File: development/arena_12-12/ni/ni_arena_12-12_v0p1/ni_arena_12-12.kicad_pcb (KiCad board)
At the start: 4 copper layers, 228.6 x 228.6 mm, 54 parts, among them J1 Barrel_Jack, J2 NI_TE_68pos, P1 CONN15, P10 CONN15, P11 CONN15, P12 CONN15, P2 CONN15, P3 CONN15, P4 CONN15, P5 CONN15, P6 CONN15, P7 CONN15, P8 CONN15, P9 CONN15, Q2 MOSFET_NCHAN, SW1 SW_SPDT, U1 TXB0108PW, U2 TXB0108PW, U3 TXB0108PW, U4 TXB0108PW, U5 TXB0108PW, U6 AP2112K-3.3

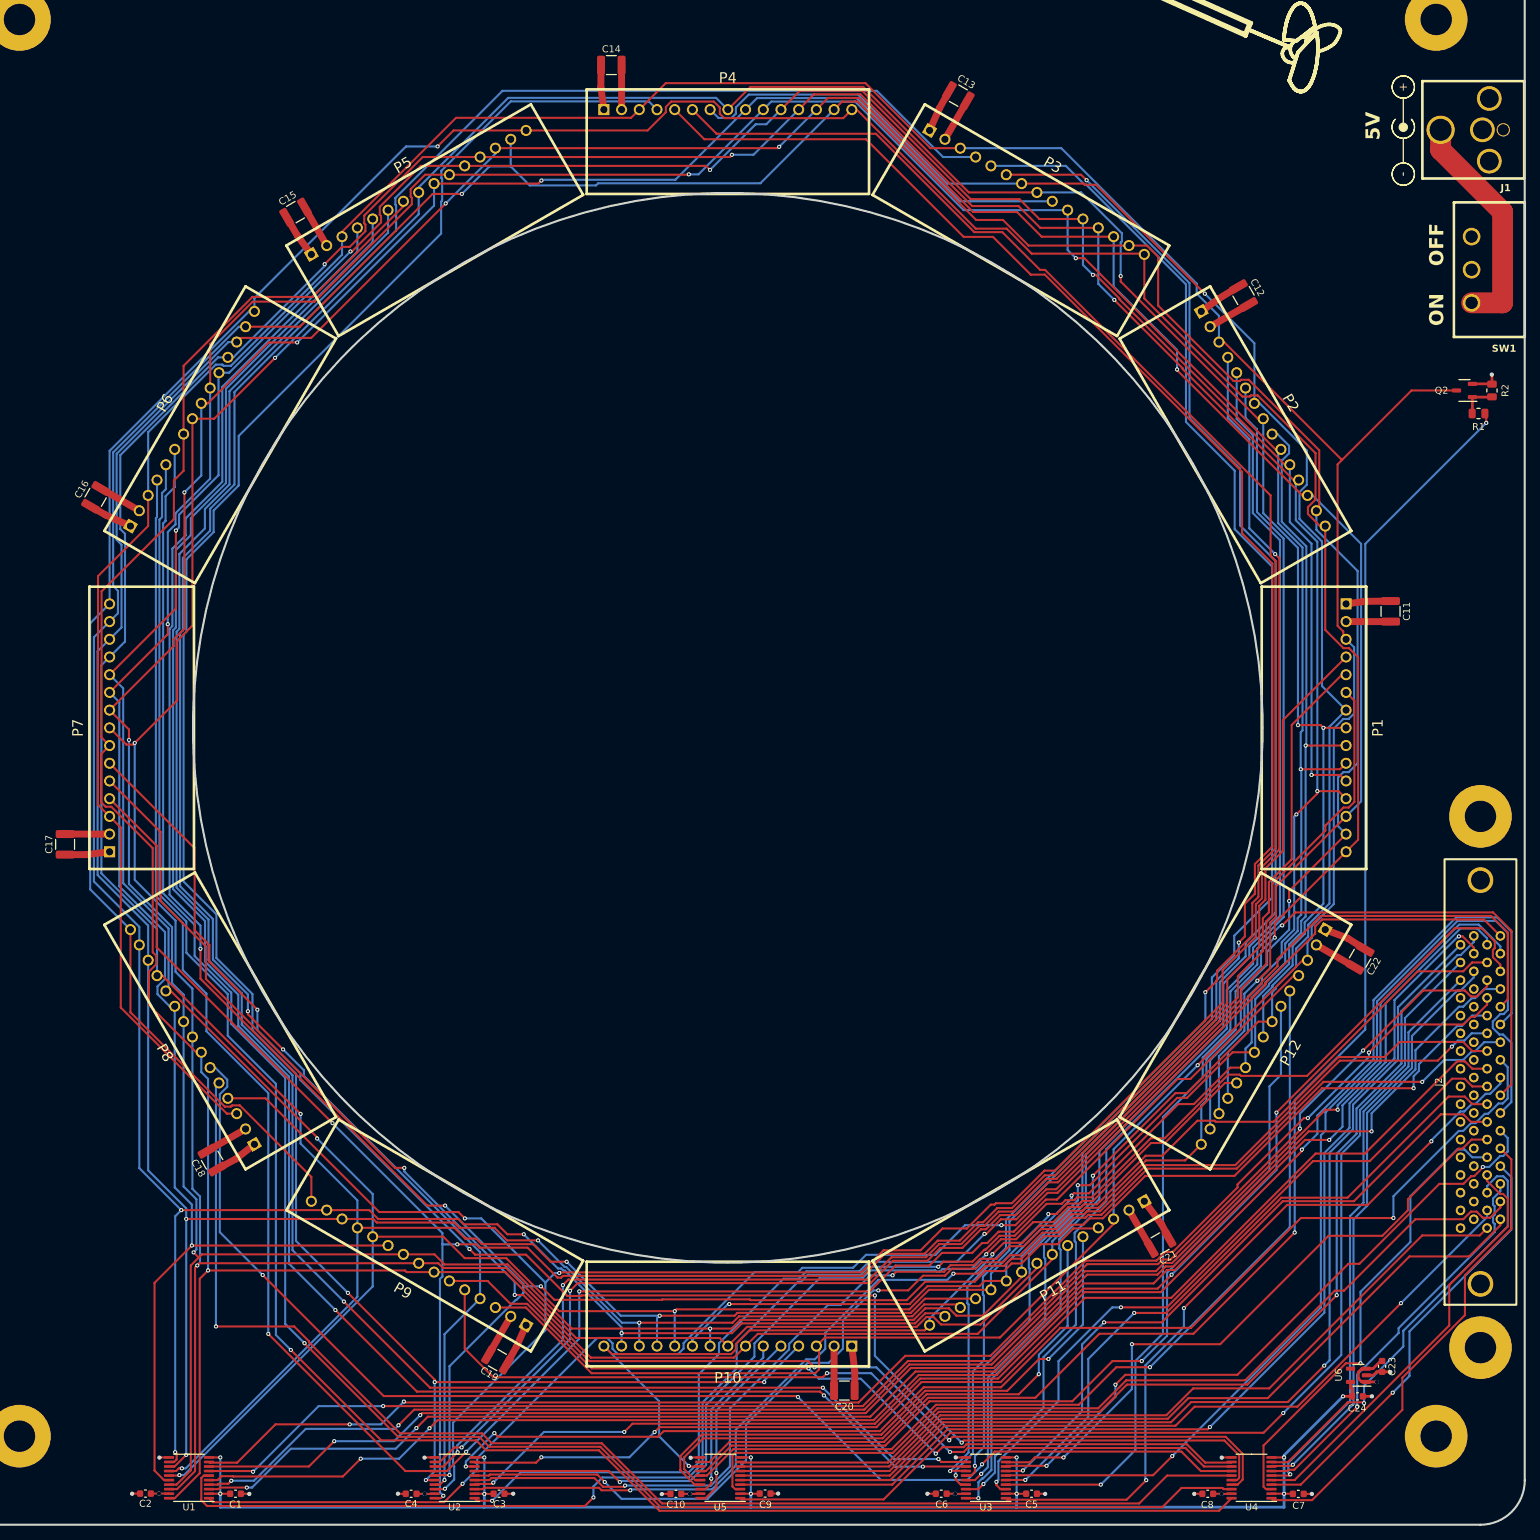
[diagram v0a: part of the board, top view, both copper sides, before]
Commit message: Worked on schematic adding series termination resistors and buffers.
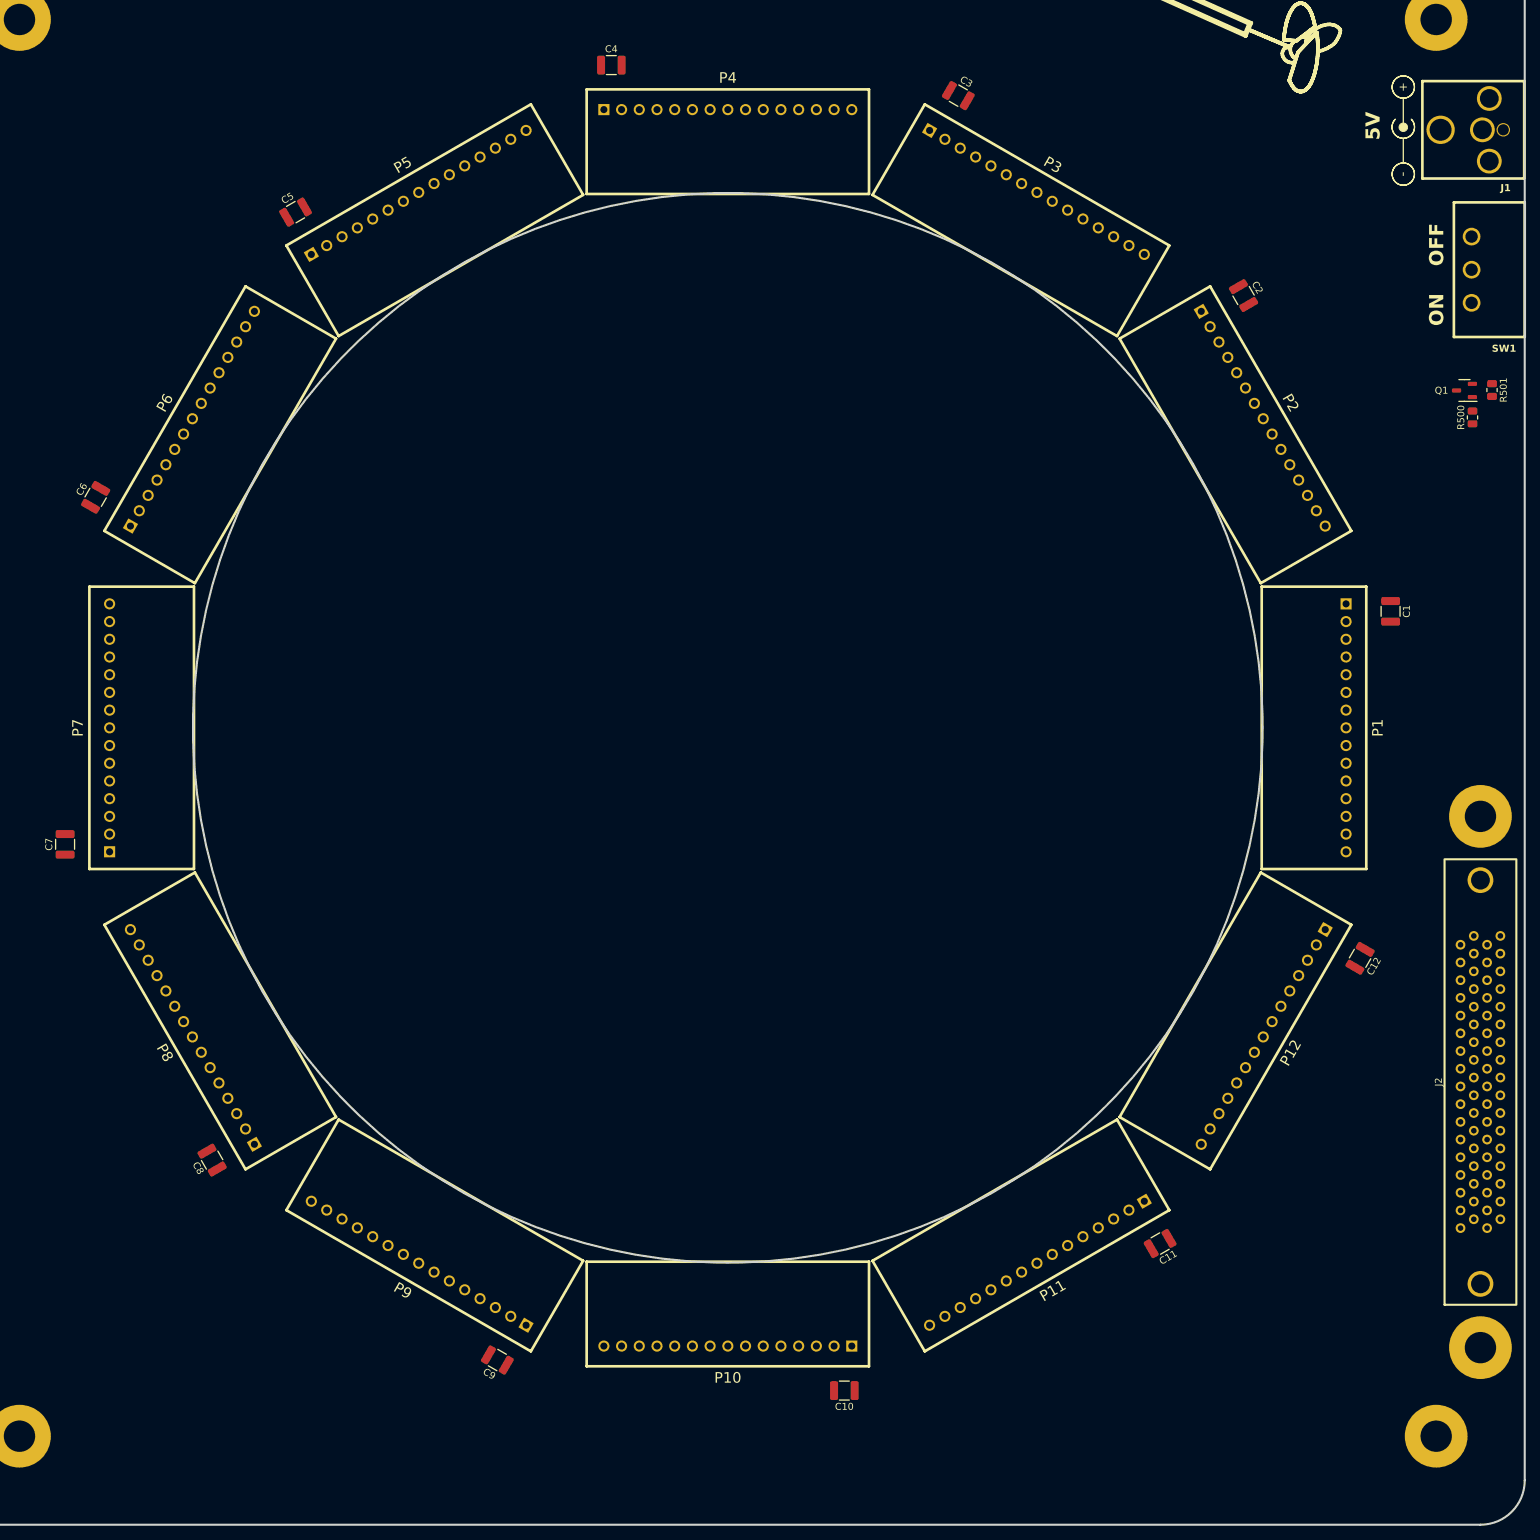
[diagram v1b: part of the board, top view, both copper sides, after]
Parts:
- removed the C1 at (107.2, 287.7)
- removed the C10 at (170.3, 287.7)
- removed the C2 at (94.3, 287.6)
- removed C23, C24: 10uF, Capacitor_SMD:C_0603_1608Metric
- removed the C3 at (145.0, 287.7)
- removed the C4 at (132.4, 287.7)
- removed the C5 at (221.4, 287.7)
- removed the C6 at (208.4, 287.7)
- removed the C7 at (259.6, 287.7)
- removed the C8 at (246.6, 287.7)
- removed the C9 at (183.1, 287.6)
- removed R1: 200, Resistor_SMD:R_0805_2012Metric
- removed R2: 20k, Resistor_SMD:R_0805_2012Metric
- removed U1, U2, U3, U4, U5: TXB0108PW, Package_SO:TSSOP-20_4.4x6.5mm_P0.65mm
- removed U6: AP2112K-3.3, Package_TO_SOT_SMD:SOT-23-5
- added R500: 200, Resistor_SMD:R_0805_2012Metric, F.Cu at (284.6, 133.3)
- added R501: 20k, Resistor_SMD:R_0805_2012Metric, F.Cu at (287.4, 129.3)
- renumbered C11 to C1, C20 to C10, C21 to C11, C22 to C12, C12 to C2, C13 to C3, C14 to C4, C15 to C5, C16 to C6, C17 to C7, C18 to C8, C19 to C9, Q2 to Q1
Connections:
- net Net-(SW1-A) renamed /Power & Voltage Regulators/SW_5V
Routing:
- net /Level Shifters/PAN5V.CS_07: track 608.7 -> 0.00 mm, vias 6 -> 0
- net /Level Shifters/PAN5V.CS_00: track 605.9 -> 0.00 mm, vias 3 -> 0
- net /Level Shifters/PAN5V.CS_01: track 601.7 -> 0.00 mm, vias 6 -> 0
- net /Level Shifters/PAN5V.CS_03: track 599.0 -> 0.00 mm, vias 7 -> 0
- net /Level Shifters/PAN5V.CS_06: track 598.2 -> 0.00 mm, vias 8 -> 0
- net /Level Shifters/PAN5V.CS_02: track 596.4 -> 0.00 mm, vias 8 -> 0
- net /Level Shifters/PAN5V.CS_05: track 594.7 -> 0.00 mm, vias 9 -> 0
- net /Level Shifters/PAN5V.CS_04: track 592.5 -> 0.00 mm, vias 9 -> 0
- net /Level Shifters/PAN5V.EXT_INT: track 581.4 -> 0.00 mm, vias 4 -> 0
- net /Panel Headers/RESET: track 579.7 -> 0.00 mm, vias 1 -> 0
- net /Level Shifters/PAN5V.SCK_05: track 318.6 -> 0.00 mm, vias 3 -> 0
- net /Level Shifters/PAN5V.SCK_02: track 311.9 -> 0.00 mm, vias 3 -> 0
- net /Level Shifters/PAN5V.SCK_03: track 309.9 -> 0.00 mm, vias 4 -> 0
- net /Level Shifters/PAN5V.SCK_00: track 309.1 -> 0.00 mm, vias 3 -> 0
- net /Level Shifters/PAN5V.SCK_04: track 306.8 -> 0.00 mm, vias 4 -> 0
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
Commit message: Wored on layout for 12-12 NI arena with schmitt buffers.
Worked on layout for schmitt buffers and series term. resitors around
at the base of a panel column.
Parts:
- removed R500: 200, Resistor_SMD:R_0805_2012Metric
- removed R501: 20k, Resistor_SMD:R_0805_2012Metric
- added C100: 0.1uF, Capacitor_SMD:C_0402_1005Metric, F.Cu at (422.1, 25.1)
- added C101: 0.1uF, Capacitor_SMD:C_0402_1005Metric, F.Cu at (422.1, 27.1)
- added C102: 0.1uF, Capacitor_SMD:C_0402_1005Metric, F.Cu at (422.1, 29.0)
- added C103: 0.1uF, Capacitor_SMD:C_0402_1005Metric, F.Cu at (422.1, 31.0)
- added C104: 0.1uF, Capacitor_SMD:C_0402_1005Metric, F.Cu at (422.1, 33.0)
- added C105: 0.1uF, Capacitor_SMD:C_0402_1005Metric, F.Cu at (422.1, 34.9)
- added C106: 0.1uF, Capacitor_SMD:C_0402_1005Metric, F.Cu at (422.1, 36.9)
- added C107: 0.1uF, Capacitor_SMD:C_0402_1005Metric, F.Cu at (458.9, 5.04)
- added C108: 0.1uF, Capacitor_SMD:C_0402_1005Metric, F.Cu at (458.9, 7.01)
- added C109: 0.1uF, Capacitor_SMD:C_0402_1005Metric, F.Cu at (458.9, 8.98)
- added C110: 0.1uF, Capacitor_SMD:C_0402_1005Metric, F.Cu at (458.9, 10.9)
- added C111: 0.1uF, Capacitor_SMD:C_0402_1005Metric, F.Cu at (458.9, 12.9)
- added C112: 0.1uF, Capacitor_SMD:C_0402_1005Metric, F.Cu at (458.9, 14.9)
- added C113: 0.1uF, Capacitor_SMD:C_0402_1005Metric, F.Cu at (458.9, 16.9)
- added C114: 0.1uF, Capacitor_SMD:C_0402_1005Metric, F.Cu at (458.9, 18.8)
- added C115: 0.1uF, Capacitor_SMD:C_0402_1005Metric, F.Cu at (458.9, 20.8)
- added C116: 0.1uF, Capacitor_SMD:C_0402_1005Metric, F.Cu at (458.9, 22.8)
- added C117: 0.1uF, Capacitor_SMD:C_0402_1005Metric, F.Cu at (461.8, 5.04)
- added C118: 0.1uF, Capacitor_SMD:C_0402_1005Metric, F.Cu at (461.8, 7.01)
- added C119: 0.1uF, Capacitor_SMD:C_0402_1005Metric, F.Cu at (461.8, 8.98)
- added C120: 0.1uF, Capacitor_SMD:C_0402_1005Metric, F.Cu at (461.8, 10.9)
- added C121: 0.1uF, Capacitor_SMD:C_0402_1005Metric, F.Cu at (461.8, 12.9)
- added C122: 0.1uF, Capacitor_SMD:C_0402_1005Metric, F.Cu at (461.8, 14.9)
- added C123: 0.1uF, Capacitor_SMD:C_0402_1005Metric, F.Cu at (461.8, 16.9)
- added C124: 0.1uF, Capacitor_SMD:C_0402_1005Metric, F.Cu at (461.8, 18.8)
- added C125: 0.1uF, Capacitor_SMD:C_0402_1005Metric, F.Cu at (461.8, 20.8)
- added C126: 0.1uF, Capacitor_SMD:C_0402_1005Metric, F.Cu at (461.8, 22.8)
- added C127: 0.1uF, Capacitor_SMD:C_0402_1005Metric, F.Cu at (464.7, 5.04)
- added C128: 0.1uF, Capacitor_SMD:C_0402_1005Metric, F.Cu at (464.7, 7.01)
- added C129: 0.1uF, Capacitor_SMD:C_0402_1005Metric, F.Cu at (464.7, 8.98)
- added C13: 10uF, Capacitor_SMD:C_1206_3216Metric, F.Cu at (443.7, 44.0)
- added C130: 0.1uF, Capacitor_SMD:C_0402_1005Metric, F.Cu at (464.7, 10.9)
- added C131: 0.1uF, Capacitor_SMD:C_0402_1005Metric, F.Cu at (464.7, 12.9)
- added C132: 0.1uF, Capacitor_SMD:C_0402_1005Metric, F.Cu at (464.7, 14.9)
- added C133: 0.1uF, Capacitor_SMD:C_0402_1005Metric, F.Cu at (464.7, 16.9)
- added C134: 0.1uF, Capacitor_SMD:C_0402_1005Metric, F.Cu at (464.7, 18.8)
- added C135: 0.1uF, Capacitor_SMD:C_0402_1005Metric, F.Cu at (464.7, 20.8)
- added C136: 0.1uF, Capacitor_SMD:C_0402_1005Metric, F.Cu at (464.7, 22.8)
- added C137: 0.1uF, Capacitor_SMD:C_0402_1005Metric, F.Cu at (467.6, 5.04)
- added C138: 0.1uF, Capacitor_SMD:C_0402_1005Metric, F.Cu at (467.6, 7.01)
- added C139: 0.1uF, Capacitor_SMD:C_0402_1005Metric, F.Cu at (467.6, 8.98)
- added C14: 10uF, Capacitor_SMD:C_1206_3216Metric, F.Cu at (443.7, 47.3)
- added C140: 0.1uF, Capacitor_SMD:C_0402_1005Metric, F.Cu at (467.6, 10.9)
- added C15: 0.1uF, Capacitor_SMD:C_0402_1005Metric, F.Cu at (453.2, 5.04)
- added C16: 0.1uF, Capacitor_SMD:C_0402_1005Metric, F.Cu at (453.2, 7.01)
- added C17: 0.1uF, Capacitor_SMD:C_0402_1005Metric, F.Cu at (453.2, 8.98)
- added C18: 0.1uF, Capacitor_SMD:C_0402_1005Metric, F.Cu at (453.2, 10.9)
- added C19: 0.1uF, Capacitor_SMD:C_0402_1005Metric, F.Cu at (453.2, 12.9)
- added C20: 0.1uF, Capacitor_SMD:C_0402_1005Metric, F.Cu at (453.2, 14.9)
- added C21: 0.1uF, Capacitor_SMD:C_0402_1005Metric, F.Cu at (453.2, 16.9)
- added C22: 0.1uF, Capacitor_SMD:C_0402_1005Metric, F.Cu at (453.2, 18.8)
- added C23: 0.1uF, Capacitor_SMD:C_0402_1005Metric, F.Cu at (453.2, 20.8)
- added C24: 0.1uF, Capacitor_SMD:C_0402_1005Metric, F.Cu at (453.2, 22.8)
- added C25: 0.1uF, Capacitor_SMD:C_0402_1005Metric, F.Cu at (456.1, 5.04)
- added C26: 0.1uF, Capacitor_SMD:C_0402_1005Metric, F.Cu at (456.1, 7.01)
- added C27: 0.1uF, Capacitor_SMD:C_0402_1005Metric, F.Cu at (456.1, 8.98)
- added C28: 0.1uF, Capacitor_SMD:C_0402_1005Metric, F.Cu at (456.1, 10.9)
- added C29: 0.1uF, Capacitor_SMD:C_0402_1005Metric, F.Cu at (456.1, 12.9)
- added C30: 0.1uF, Capacitor_SMD:C_0402_1005Metric, F.Cu at (456.1, 14.9)
- added C31: 0.1uF, Capacitor_SMD:C_0402_1005Metric, F.Cu at (456.1, 16.9)
- added C32: 0.1uF, Capacitor_SMD:C_0402_1005Metric, F.Cu at (456.1, 18.8)
- added C33: 0.1uF, Capacitor_SMD:C_0402_1005Metric, F.Cu at (456.1, 20.8)
- added C34: 0.1uF, Capacitor_SMD:C_0402_1005Metric, F.Cu at (456.1, 22.8)
- added C35: 0.1uF, Capacitor_SMD:C_0402_1005Metric, F.Cu at (271.1, 168.9)
- added C36: 0.1uF, Capacitor_SMD:C_0402_1005Metric, F.Cu at (271.1, 176.6)
- added C37: 0.1uF, Capacitor_SMD:C_0402_1005Metric, F.Cu at (271.1, 181.7)
- added C38: 0.1uF, Capacitor_SMD:C_0402_1005Metric, F.Cu at (271.1, 186.7)
- added C39: 0.1uF, Capacitor_SMD:C_0402_1005Metric, F.Cu at (271.0, 191.8)
- added C40: 0.1uF, Capacitor_SMD:C_0402_1005Metric, F.Cu at (271.0, 197.3)
- added C41: 0.1uF, Capacitor_SMD:C_0402_1005Metric, F.Cu at (407.7, 27.1)
- added C42: 0.1uF, Capacitor_SMD:C_0402_1005Metric, F.Cu at (407.7, 29.0)
- added C43: 0.1uF, Capacitor_SMD:C_0402_1005Metric, F.Cu at (407.7, 31.0)
- added C44: 0.1uF, Capacitor_SMD:C_0402_1005Metric, F.Cu at (407.7, 33.0)
- added C45: 0.1uF, Capacitor_SMD:C_0402_1005Metric, F.Cu at (407.7, 34.9)
- added C46: 0.1uF, Capacitor_SMD:C_0402_1005Metric, F.Cu at (407.7, 36.9)
- added C47: 0.1uF, Capacitor_SMD:C_0402_1005Metric, F.Cu at (410.6, 15.2)
- added C48: 0.1uF, Capacitor_SMD:C_0402_1005Metric, F.Cu at (410.6, 17.2)
- added C49: 0.1uF, Capacitor_SMD:C_0402_1005Metric, F.Cu at (410.6, 19.2)
- added C50: 0.1uF, Capacitor_SMD:C_0402_1005Metric, F.Cu at (410.6, 21.1)
- added C51: 0.1uF, Capacitor_SMD:C_0402_1005Metric, F.Cu at (410.6, 23.1)
- added C52: 0.1uF, Capacitor_SMD:C_0402_1005Metric, F.Cu at (410.6, 25.1)
- added C53: 0.1uF, Capacitor_SMD:C_0402_1005Metric, F.Cu at (410.6, 27.1)
- added C54: 0.1uF, Capacitor_SMD:C_0402_1005Metric, F.Cu at (410.6, 29.0)
- added C55: 0.1uF, Capacitor_SMD:C_0402_1005Metric, F.Cu at (410.6, 31.0)
- added C56: 0.1uF, Capacitor_SMD:C_0402_1005Metric, F.Cu at (410.6, 33.0)
- added C57: 0.1uF, Capacitor_SMD:C_0402_1005Metric, F.Cu at (410.6, 34.9)
- added C58: 0.1uF, Capacitor_SMD:C_0402_1005Metric, F.Cu at (410.6, 36.9)
- added C59: 0.1uF, Capacitor_SMD:C_0402_1005Metric, F.Cu at (413.5, 15.2)
- added C60: 0.1uF, Capacitor_SMD:C_0402_1005Metric, F.Cu at (413.5, 17.2)
- added C61: 0.1uF, Capacitor_SMD:C_0402_1005Metric, F.Cu at (413.5, 19.2)
- added C62: 0.1uF, Capacitor_SMD:C_0402_1005Metric, F.Cu at (413.5, 21.1)
- added C63: 0.1uF, Capacitor_SMD:C_0402_1005Metric, F.Cu at (413.5, 23.1)
- added C64: 0.1uF, Capacitor_SMD:C_0402_1005Metric, F.Cu at (413.5, 25.1)
- added C65: 0.1uF, Capacitor_SMD:C_0402_1005Metric, F.Cu at (413.5, 27.1)
- added C66: 0.1uF, Capacitor_SMD:C_0402_1005Metric, F.Cu at (413.5, 29.0)
- added C67: 0.1uF, Capacitor_SMD:C_0402_1005Metric, F.Cu at (413.5, 31.0)
- added C68: 0.1uF, Capacitor_SMD:C_0402_1005Metric, F.Cu at (413.5, 33.0)
- added C69: 0.1uF, Capacitor_SMD:C_0402_1005Metric, F.Cu at (413.5, 34.9)
- added C70: 0.1uF, Capacitor_SMD:C_0402_1005Metric, F.Cu at (413.5, 36.9)
- added C71: 0.1uF, Capacitor_SMD:C_0402_1005Metric, F.Cu at (416.4, 15.2)
- added C72: 0.1uF, Capacitor_SMD:C_0402_1005Metric, F.Cu at (416.4, 17.2)
- added C73: 0.1uF, Capacitor_SMD:C_0402_1005Metric, F.Cu at (416.4, 19.2)
- added C74: 0.1uF, Capacitor_SMD:C_0402_1005Metric, F.Cu at (416.4, 21.1)
- added C75: 0.1uF, Capacitor_SMD:C_0402_1005Metric, F.Cu at (416.4, 23.1)
- added C76: 0.1uF, Capacitor_SMD:C_0402_1005Metric, F.Cu at (416.4, 25.1)
- added C77: 0.1uF, Capacitor_SMD:C_0402_1005Metric, F.Cu at (416.4, 27.1)
- added C78: 0.1uF, Capacitor_SMD:C_0402_1005Metric, F.Cu at (416.4, 29.0)
- added C79: 0.1uF, Capacitor_SMD:C_0402_1005Metric, F.Cu at (416.4, 31.0)
- added C80: 0.1uF, Capacitor_SMD:C_0402_1005Metric, F.Cu at (416.4, 33.0)
- added C81: 0.1uF, Capacitor_SMD:C_0402_1005Metric, F.Cu at (416.4, 34.9)
- added C82: 0.1uF, Capacitor_SMD:C_0402_1005Metric, F.Cu at (416.4, 36.9)
- added C83: 0.1uF, Capacitor_SMD:C_0402_1005Metric, F.Cu at (419.2, 15.2)
- added C84: 0.1uF, Capacitor_SMD:C_0402_1005Metric, F.Cu at (419.2, 17.2)
- added C85: 0.1uF, Capacitor_SMD:C_0402_1005Metric, F.Cu at (419.2, 19.2)
- added C86: 0.1uF, Capacitor_SMD:C_0402_1005Metric, F.Cu at (419.2, 21.1)
- added C87: 0.1uF, Capacitor_SMD:C_0402_1005Metric, F.Cu at (419.2, 23.1)
- added C88: 0.1uF, Capacitor_SMD:C_0402_1005Metric, F.Cu at (419.2, 25.1)
- added C89: 0.1uF, Capacitor_SMD:C_0402_1005Metric, F.Cu at (419.2, 27.1)
- added C90: 0.1uF, Capacitor_SMD:C_0402_1005Metric, F.Cu at (419.2, 29.0)
- added C91: 0.1uF, Capacitor_SMD:C_0402_1005Metric, F.Cu at (419.2, 31.0)
- added C92: 0.1uF, Capacitor_SMD:C_0402_1005Metric, F.Cu at (419.2, 33.0)
- added C93: 0.1uF, Capacitor_SMD:C_0402_1005Metric, F.Cu at (419.2, 34.9)
- added C94: 0.1uF, Capacitor_SMD:C_0402_1005Metric, F.Cu at (419.2, 36.9)
- added C95: 0.1uF, Capacitor_SMD:C_0402_1005Metric, F.Cu at (422.1, 15.2)
- added C96: 0.1uF, Capacitor_SMD:C_0402_1005Metric, F.Cu at (422.1, 17.2)
- added C97: 0.1uF, Capacitor_SMD:C_0402_1005Metric, F.Cu at (422.1, 19.2)
- added C98: 0.1uF, Capacitor_SMD:C_0402_1005Metric, F.Cu at (422.1, 21.1)
- added C99: 0.1uF, Capacitor_SMD:C_0402_1005Metric, F.Cu at (422.1, 23.1)
- added J3: Barrel_Jack, arena_custom:DCJACK_2PIN_HIGHCURRENT, F.Cu at (95.0, 63.5)
- added R1: 33, Resistor_SMD:R_0402_1005Metric, F.Cu at (450.0, 43.3)
- added R10: 33, Resistor_SMD:R_0402_1005Metric, F.Cu at (452.9, 45.3)
- added R100: 33, Resistor_SMD:R_0402_1005Metric, F.Cu at (462.0, 3.06)
- added R101: 33, Resistor_SMD:R_0402_1005Metric, F.Cu at (464.9, -24.8)
- added R102: 33, Resistor_SMD:R_0402_1005Metric, F.Cu at (464.9, -22.8)
- added R103: 33, Resistor_SMD:R_0402_1005Metric, F.Cu at (464.9, -20.8)
- added R104: 33, Resistor_SMD:R_0402_1005Metric, F.Cu at (464.9, -18.8)
- added R105: 33, Resistor_SMD:R_0402_1005Metric, F.Cu at (464.9, -16.8)
- added R106: 33, Resistor_SMD:R_0402_1005Metric, F.Cu at (464.9, -14.8)
- added R107: 33, Resistor_SMD:R_0402_1005Metric, F.Cu at (464.9, -12.9)
- added R108: 33, Resistor_SMD:R_0402_1005Metric, F.Cu at (464.9, -10.9)
- added R109: 33, Resistor_SMD:R_0402_1005Metric, F.Cu at (464.9, -8.88)
- added R11: 33, Resistor_SMD:R_0402_1005Metric, F.Cu at (452.9, 47.3)
- added R110: 33, Resistor_SMD:R_0402_1005Metric, F.Cu at (464.9, -6.89)
- added R111: 33, Resistor_SMD:R_0402_1005Metric, F.Cu at (464.9, -4.90)
- added R112: 33, Resistor_SMD:R_0402_1005Metric, F.Cu at (464.9, -2.91)
- added R113: 33, Resistor_SMD:R_0402_1005Metric, F.Cu at (464.9, -0.92)
- added R114: 33, Resistor_SMD:R_0402_1005Metric, F.Cu at (464.9, 1.07)
- added R115: 33, Resistor_SMD:R_0402_1005Metric, F.Cu at (464.9, 3.06)
- added R116: 33, Resistor_SMD:R_0402_1005Metric, F.Cu at (467.8, -24.8)
- added R117: 33, Resistor_SMD:R_0402_1005Metric, F.Cu at (467.8, -22.8)
- added R118: 33, Resistor_SMD:R_0402_1005Metric, F.Cu at (467.8, -20.8)
- added R119: 33, Resistor_SMD:R_0402_1005Metric, F.Cu at (467.8, -18.8)
- added R12: 33, Resistor_SMD:R_0402_1005Metric, F.Cu at (452.9, 49.3)
- added R120: 33, Resistor_SMD:R_0402_1005Metric, F.Cu at (467.8, -16.8)
- added R121: 33, Resistor_SMD:R_0402_1005Metric, F.Cu at (467.8, -14.8)
- added R122: 33, Resistor_SMD:R_0402_1005Metric, F.Cu at (467.8, -12.9)
- added R123: 33, Resistor_SMD:R_0402_1005Metric, F.Cu at (467.8, -10.9)
- added R124: 33, Resistor_SMD:R_0402_1005Metric, F.Cu at (467.8, -8.88)
- added R125: 33, Resistor_SMD:R_0402_1005Metric, F.Cu at (467.8, -6.89)
- added R126: 33, Resistor_SMD:R_0402_1005Metric, F.Cu at (467.8, -4.90)
- added R127: 33, Resistor_SMD:R_0402_1005Metric, F.Cu at (467.8, -2.91)
- added R128: 33, Resistor_SMD:R_0402_1005Metric, F.Cu at (467.8, -0.92)
- added R129: 33, Resistor_SMD:R_0402_1005Metric, F.Cu at (467.8, 1.07)
- added R13: 33, Resistor_SMD:R_0402_1005Metric, F.Cu at (452.9, 51.3)
- added R130: 33, Resistor_SMD:R_0402_1005Metric, F.Cu at (467.8, 3.06)
- added R131: 33, Resistor_SMD:R_0402_1005Metric, F.Cu at (470.7, -24.8)
- added R132: 33, Resistor_SMD:R_0402_1005Metric, F.Cu at (470.7, -22.8)
- added R133: 33, Resistor_SMD:R_0402_1005Metric, F.Cu at (470.7, -20.8)
- added R134: 33, Resistor_SMD:R_0402_1005Metric, F.Cu at (470.7, -18.8)
- added R135: 33, Resistor_SMD:R_0402_1005Metric, F.Cu at (470.7, -16.8)
- added R136: 33, Resistor_SMD:R_0402_1005Metric, F.Cu at (470.7, -14.8)
- added R137: 33, Resistor_SMD:R_0402_1005Metric, F.Cu at (470.7, -12.9)
- added R138: 33, Resistor_SMD:R_0402_1005Metric, F.Cu at (470.7, -10.9)
- added R139: 33, Resistor_SMD:R_0402_1005Metric, F.Cu at (470.7, -8.88)
- added R14: 33, Resistor_SMD:R_0402_1005Metric, F.Cu at (452.9, 53.2)
- added R140: 33, Resistor_SMD:R_0402_1005Metric, F.Cu at (470.7, -6.89)
- added R141: 33, Resistor_SMD:R_0402_1005Metric, F.Cu at (470.7, -4.90)
- added R142: 33, Resistor_SMD:R_0402_1005Metric, F.Cu at (470.7, -2.91)
- added R143: 33, Resistor_SMD:R_0402_1005Metric, F.Cu at (470.7, -0.92)
- added R144: 33, Resistor_SMD:R_0402_1005Metric, F.Cu at (470.7, 1.07)
- added R145: 33, Resistor_SMD:R_0402_1005Metric, F.Cu at (470.7, 3.06)
- added R146: 33, Resistor_SMD:R_0402_1005Metric, F.Cu at (473.6, -24.8)
- added R147: 33, Resistor_SMD:R_0402_1005Metric, F.Cu at (473.6, -22.8)
- added R148: 33, Resistor_SMD:R_0402_1005Metric, F.Cu at (473.6, -20.8)
- added R149: 33, Resistor_SMD:R_0402_1005Metric, F.Cu at (473.6, -18.8)
- added R15: 33, Resistor_SMD:R_0402_1005Metric, F.Cu at (452.9, 55.2)
- added R150: 33, Resistor_SMD:R_0402_1005Metric, F.Cu at (473.6, -16.8)
- added R151: 33, Resistor_SMD:R_0402_1005Metric, F.Cu at (473.6, -14.8)
- added R152: 33, Resistor_SMD:R_0402_1005Metric, F.Cu at (473.6, -12.9)
- added R153: 33, Resistor_SMD:R_0402_1005Metric, F.Cu at (473.6, -10.9)
- added R154: 33, Resistor_SMD:R_0402_1005Metric, F.Cu at (473.6, -8.88)
- added R155: 33, Resistor_SMD:R_0402_1005Metric, F.Cu at (473.6, -6.89)
- added R156: 33, Resistor_SMD:R_0402_1005Metric, F.Cu at (473.6, -4.90)
- added R157: 33, Resistor_SMD:R_0402_1005Metric, F.Cu at (473.6, -2.91)
- added R158: 33, Resistor_SMD:R_0402_1005Metric, F.Cu at (473.6, -0.92)
- added R159: 33, Resistor_SMD:R_0402_1005Metric, F.Cu at (473.6, 1.07)
- added R16: 33, Resistor_SMD:R_0402_1005Metric, F.Cu at (452.9, 57.2)
- added R160: 33, Resistor_SMD:R_0402_1005Metric, F.Cu at (473.6, 3.06)
- added R161: 33, Resistor_SMD:R_0402_1005Metric, F.Cu at (476.5, -24.8)
- added R162: 33, Resistor_SMD:R_0402_1005Metric, F.Cu at (476.5, -22.8)
- added R163: 33, Resistor_SMD:R_0402_1005Metric, F.Cu at (476.5, -20.8)
- added R164: 33, Resistor_SMD:R_0402_1005Metric, F.Cu at (476.5, -18.8)
- added R165: 33, Resistor_SMD:R_0402_1005Metric, F.Cu at (476.5, -16.8)
- added R166: 33, Resistor_SMD:R_0402_1005Metric, F.Cu at (476.5, -14.8)
- added R167: 33, Resistor_SMD:R_0402_1005Metric, F.Cu at (476.5, -12.9)
- added R168: 33, Resistor_SMD:R_0402_1005Metric, F.Cu at (476.5, -10.9)
- added R169: 33, Resistor_SMD:R_0402_1005Metric, F.Cu at (476.5, -8.88)
- added R17: 33, Resistor_SMD:R_0402_1005Metric, F.Cu at (455.8, 43.3)
- added R170: 33, Resistor_SMD:R_0402_1005Metric, F.Cu at (476.5, -6.89)
- added R171: 33, Resistor_SMD:R_0402_1005Metric, F.Cu at (476.5, -4.90)
- added R172: 33, Resistor_SMD:R_0402_1005Metric, F.Cu at (476.5, -2.91)
- added R173: 33, Resistor_SMD:R_0402_1005Metric, F.Cu at (476.5, -0.92)
- added R174: 33, Resistor_SMD:R_0402_1005Metric, F.Cu at (476.5, 1.07)
- added R175: 33, Resistor_SMD:R_0402_1005Metric, F.Cu at (378.7, 39.1)
- added R176: 33, Resistor_SMD:R_0402_1005Metric, F.Cu at (378.7, 41.1)
- added R177: 33, Resistor_SMD:R_0402_1005Metric, F.Cu at (378.7, 43.1)
- added R178: 33, Resistor_SMD:R_0402_1005Metric, F.Cu at (381.6, 15.2)
- added R179: 33, Resistor_SMD:R_0402_1005Metric, F.Cu at (381.6, 17.2)
- added R18: 33, Resistor_SMD:R_0402_1005Metric, F.Cu at (455.8, 45.3)
- added R180: 33, Resistor_SMD:R_0402_1005Metric, F.Cu at (381.6, 19.2)
- added R181: 33, Resistor_SMD:R_0402_1005Metric, F.Cu at (381.6, 21.2)
- added R182: 33, Resistor_SMD:R_0402_1005Metric, F.Cu at (381.6, 23.2)
- added R183: 33, Resistor_SMD:R_0402_1005Metric, F.Cu at (381.6, 25.2)
- added R184: 33, Resistor_SMD:R_0402_1005Metric, F.Cu at (381.6, 27.2)
- added R185: 33, Resistor_SMD:R_0402_1005Metric, F.Cu at (381.6, 29.2)
- added R186: 33, Resistor_SMD:R_0402_1005Metric, F.Cu at (381.6, 31.2)
- added R187: 33, Resistor_SMD:R_0402_1005Metric, F.Cu at (381.6, 33.2)
- added R188: 33, Resistor_SMD:R_0402_1005Metric, F.Cu at (381.6, 35.1)
- added R189: 33, Resistor_SMD:R_0402_1005Metric, F.Cu at (381.6, 37.1)
- added R19: 33, Resistor_SMD:R_0402_1005Metric, F.Cu at (455.8, 47.3)
- added R190: 33, Resistor_SMD:R_0402_1005Metric, F.Cu at (381.6, 39.1)
- added R191: 33, Resistor_SMD:R_0402_1005Metric, F.Cu at (381.6, 41.1)
- added R192: 33, Resistor_SMD:R_0402_1005Metric, F.Cu at (381.6, 43.1)
- added R193: 33, Resistor_SMD:R_0402_1005Metric, F.Cu at (384.5, 15.2)
- added R194: 33, Resistor_SMD:R_0402_1005Metric, F.Cu at (384.5, 17.2)
- added R195: 33, Resistor_SMD:R_0402_1005Metric, F.Cu at (384.5, 19.2)
- added R196: 33, Resistor_SMD:R_0402_1005Metric, F.Cu at (384.5, 21.2)
- added R197: 33, Resistor_SMD:R_0402_1005Metric, F.Cu at (384.5, 23.2)
- added R198: 33, Resistor_SMD:R_0402_1005Metric, F.Cu at (384.5, 25.2)
- added R199: 33, Resistor_SMD:R_0402_1005Metric, F.Cu at (384.5, 27.2)
- added R2: 33, Resistor_SMD:R_0402_1005Metric, F.Cu at (450.0, 45.3)
- added R20: 33, Resistor_SMD:R_0402_1005Metric, F.Cu at (455.8, 49.3)
- added R200: 33, Resistor_SMD:R_0402_1005Metric, F.Cu at (384.5, 29.2)
- added R201: 33, Resistor_SMD:R_0402_1005Metric, F.Cu at (384.5, 31.2)
- added R202: 33, Resistor_SMD:R_0402_1005Metric, F.Cu at (384.5, 33.2)
- added R203: 33, Resistor_SMD:R_0402_1005Metric, F.Cu at (384.5, 35.1)
- added R204: 33, Resistor_SMD:R_0402_1005Metric, F.Cu at (384.5, 37.1)
- added R205: 33, Resistor_SMD:R_0402_1005Metric, F.Cu at (384.5, 39.1)
- added R206: 33, Resistor_SMD:R_0402_1005Metric, F.Cu at (384.5, 41.1)
- added R207: 33, Resistor_SMD:R_0402_1005Metric, F.Cu at (384.5, 43.1)
- added R208: 33, Resistor_SMD:R_0402_1005Metric, F.Cu at (387.4, 15.2)
- added R209: 33, Resistor_SMD:R_0402_1005Metric, F.Cu at (387.4, 17.2)
- added R21: 33, Resistor_SMD:R_0402_1005Metric, F.Cu at (455.8, 51.3)
- added R210: 33, Resistor_SMD:R_0402_1005Metric, F.Cu at (387.4, 19.2)
- added R211: 33, Resistor_SMD:R_0402_1005Metric, F.Cu at (387.4, 21.2)
- added R212: 33, Resistor_SMD:R_0402_1005Metric, F.Cu at (387.4, 23.2)
- added R213: 33, Resistor_SMD:R_0402_1005Metric, F.Cu at (387.4, 25.2)
- added R214: 33, Resistor_SMD:R_0402_1005Metric, F.Cu at (387.4, 27.2)
- added R215: 33, Resistor_SMD:R_0402_1005Metric, F.Cu at (387.4, 29.2)
- added R216: 33, Resistor_SMD:R_0402_1005Metric, F.Cu at (387.4, 31.2)
- added R217: 33, Resistor_SMD:R_0402_1005Metric, F.Cu at (387.4, 33.2)
- added R218: 33, Resistor_SMD:R_0402_1005Metric, F.Cu at (387.4, 35.1)
- added R219: 33, Resistor_SMD:R_0402_1005Metric, F.Cu at (387.4, 37.1)
- added R22: 33, Resistor_SMD:R_0402_1005Metric, F.Cu at (455.8, 53.2)
- added R220: 33, Resistor_SMD:R_0402_1005Metric, F.Cu at (387.4, 39.1)
- added R221: 33, Resistor_SMD:R_0402_1005Metric, F.Cu at (387.4, 41.1)
- added R222: 33, Resistor_SMD:R_0402_1005Metric, F.Cu at (387.4, 43.1)
- added R223: 33, Resistor_SMD:R_0402_1005Metric, F.Cu at (390.3, 15.2)
- added R224: 33, Resistor_SMD:R_0402_1005Metric, F.Cu at (390.3, 17.2)
- added R225: 33, Resistor_SMD:R_0402_1005Metric, F.Cu at (390.3, 19.2)
- added R226: 33, Resistor_SMD:R_0402_1005Metric, F.Cu at (390.3, 21.2)
- added R227: 33, Resistor_SMD:R_0402_1005Metric, F.Cu at (390.3, 23.2)
- added R228: 33, Resistor_SMD:R_0402_1005Metric, F.Cu at (390.3, 25.2)
- added R229: 33, Resistor_SMD:R_0402_1005Metric, F.Cu at (390.3, 27.2)
- added R23: 33, Resistor_SMD:R_0402_1005Metric, F.Cu at (455.8, 55.2)
- added R230: 33, Resistor_SMD:R_0402_1005Metric, F.Cu at (390.3, 29.2)
- added R231: 33, Resistor_SMD:R_0402_1005Metric, F.Cu at (390.3, 31.2)
- added R232: 33, Resistor_SMD:R_0402_1005Metric, F.Cu at (390.3, 33.2)
- added R233: 33, Resistor_SMD:R_0402_1005Metric, F.Cu at (390.3, 35.1)
- added R234: 33, Resistor_SMD:R_0402_1005Metric, F.Cu at (390.3, 37.1)
- added R235: 33, Resistor_SMD:R_0402_1005Metric, F.Cu at (390.3, 39.1)
- added R236: 33, Resistor_SMD:R_0402_1005Metric, F.Cu at (390.3, 41.1)
- added R237: 33, Resistor_SMD:R_0402_1005Metric, F.Cu at (390.3, 43.1)
- added R238: 33, Resistor_SMD:R_0402_1005Metric, F.Cu at (393.2, 15.2)
- added R239: 33, Resistor_SMD:R_0402_1005Metric, F.Cu at (393.2, 17.2)
- added R24: 33, Resistor_SMD:R_0402_1005Metric, F.Cu at (455.8, 57.2)
- added R240: 33, Resistor_SMD:R_0402_1005Metric, F.Cu at (393.2, 19.2)
- added R241: 33, Resistor_SMD:R_0402_1005Metric, F.Cu at (393.2, 21.2)
- added R242: 33, Resistor_SMD:R_0402_1005Metric, F.Cu at (393.2, 23.2)
- added R243: 33, Resistor_SMD:R_0402_1005Metric, F.Cu at (393.2, 25.2)
- added R244: 33, Resistor_SMD:R_0402_1005Metric, F.Cu at (393.2, 27.2)
- added R245: 33, Resistor_SMD:R_0402_1005Metric, F.Cu at (393.2, 29.2)
- added R246: 33, Resistor_SMD:R_0402_1005Metric, F.Cu at (393.2, 31.2)
- added R247: 33, Resistor_SMD:R_0402_1005Metric, F.Cu at (393.2, 33.2)
- added R248: 33, Resistor_SMD:R_0402_1005Metric, F.Cu at (393.2, 35.1)
- added R249: 33, Resistor_SMD:R_0402_1005Metric, F.Cu at (393.2, 37.1)
- added R25: 33, Resistor_SMD:R_0402_1005Metric, F.Cu at (458.7, 43.3)
- added R250: 33, Resistor_SMD:R_0402_1005Metric, F.Cu at (393.2, 39.1)
- added R251: 33, Resistor_SMD:R_0402_1005Metric, F.Cu at (393.2, 41.1)
- added R252: 33, Resistor_SMD:R_0402_1005Metric, F.Cu at (393.2, 43.1)
- added R253: 33, Resistor_SMD:R_0402_1005Metric, F.Cu at (396.1, 15.2)
- added R254: 33, Resistor_SMD:R_0402_1005Metric, F.Cu at (396.1, 17.2)
- added R255: 33, Resistor_SMD:R_0402_1005Metric, F.Cu at (396.1, 19.2)
- added R256: 33, Resistor_SMD:R_0402_1005Metric, F.Cu at (396.1, 21.2)
- added R257: 33, Resistor_SMD:R_0402_1005Metric, F.Cu at (396.1, 23.2)
- added R258: 33, Resistor_SMD:R_0402_1005Metric, F.Cu at (396.1, 25.2)
- added R259: 33, Resistor_SMD:R_0402_1005Metric, F.Cu at (396.1, 27.2)
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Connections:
- J2 pad 29: /Level Shifters/PAN3V.MOSI_07 -> Net-(J2-Pin_29)
- J2 pad 30: /Level Shifters/PAN3V.MOSI_08 -> Net-(J2-Pin_30)
- J2 pad 31: /Level Shifters/PAN3V.MOSI_09 -> Net-(J2-Pin_31)
- J2 pad 32: /Level Shifters/PAN3V.MOSI_10 -> Net-(J2-Pin_32)
- J2 pad 33: /Level Shifters/PAN3V.MOSI_11 -> Net-(J2-Pin_33)
- J2 pad 34: /Level Shifters/PAN3V.RESET -> Net-(J2-Pin_34)
- J2 pad 35: /Level Shifters/PAN3V.EXT_INT -> Net-(J2-Pin_35)
- J2 pad 36: /Level Shifters/PAN3V.MISO_11 -> Net-(J2-Pin_36)
- J2 pad 37: /Level Shifters/PAN3V.MISO_10 -> Net-(J2-Pin_37)
- J2 pad 38: /Level Shifters/PAN3V.MISO_09 -> Net-(J2-Pin_38)
- J2 pad 39: /Level Shifters/PAN3V.MISO_08 -> Net-(J2-Pin_39)
- J2 pad 40: /Level Shifters/PAN3V.MISO_07 -> Net-(J2-Pin_40)
- J2 pad 41: /Level Shifters/PAN3V.MISO_06 -> Net-(J2-Pin_41)
- J2 pad 42: /Level Shifters/PAN3V.MOSI_06 -> Net-(J2-Pin_42)
- J2 pad 43: /Level Shifters/PAN3V.MISO_05 -> Net-(J2-Pin_43)
- J2 pad 44: /Level Shifters/PAN3V.MOSI_05 -> Net-(J2-Pin_44)
- J2 pad 45: /Level Shifters/PAN3V.MISO_04 -> Net-(J2-Pin_45)
- J2 pad 46: /Level Shifters/PAN3V.MOSI_04 -> Net-(J2-Pin_46)
- J2 pad 47: /Level Shifters/PAN3V.MISO_03 -> Net-(J2-Pin_47)
- J2 pad 48: /Level Shifters/PAN3V.MOSI_03 -> Net-(J2-Pin_48)
- J2 pad 49: /Level Shifters/PAN3V.MISO_02 -> Net-(J2-Pin_49)
- J2 pad 50: /Level Shifters/PAN3V.MOSI_02 -> /Level Shifters/PAN3V.MISO_00
- J2 pad 51: /Level Shifters/PAN3V.MISO_01 -> Net-(J2-Pin_51)
- J2 pad 52: /Level Shifters/PAN3V.MOSI_01 -> /Level Shifters/PAN3V.MISO_01
- J2 pad 53: /Level Shifters/PAN3V.MISO_00 -> Net-(J2-Pin_53)
- J2 pad 54: /Level Shifters/PAN3V.MOSI_00 -> /Level Shifters/PAN3V.MISO_02
- J2 pad 55: /Level Shifters/PAN3V.SCK_05 -> Net-(J2-Pin_55)
- J2 pad 56: /Level Shifters/PAN3V.SCK_04 -> /Level Shifters/PAN3V.MISO_03
- J2 pad 57: /Level Shifters/PAN3V.SCK_03 -> Net-(J2-Pin_57)
- J2 pad 58: /Level Shifters/PAN3V.SCK_02 -> /Level Shifters/PAN3V.MISO_04
- J2 pad 59: /Level Shifters/PAN3V.SCK_01 -> Net-(J2-Pin_59)
- J2 pad 60: /Level Shifters/PAN3V.SCK_00 -> /Level Shifters/PAN3V.MISO_05
- J2 pad 61: /Level Shifters/PAN3V.CS_07 -> Net-(J2-Pin_61)
- J2 pad 62: /Level Shifters/PAN3V.CS_06 -> /Level Shifters/PAN3V.MISO_06
- J2 pad 63: /Level Shifters/PAN3V.CS_05 -> /Level Shifters/PAN3V.MISO_07
- J2 pad 64: /Level Shifters/PAN3V.CS_04 -> /Level Shifters/PAN3V.MISO_08
- J2 pad 65: /Level Shifters/PAN3V.CS_03 -> /Level Shifters/PAN3V.MISO_09
- J2 pad 66: /Level Shifters/PAN3V.CS_02 -> /Level Shifters/PAN3V.MISO_10
- J2 pad 67: /Level Shifters/PAN3V.CS_01 -> /Level Shifters/PAN3V.MISO_11
- J2 pad 68: /Level Shifters/PAN3V.CS_00 -> Net-(J2-Pin_68)
- P1 pad 10: /Level Shifters/PAN5V.CS_03 -> /Panel Headers/CS_03_P01
- P1 pad 11: /Level Shifters/PAN5V.CS_04 -> /Panel Headers/CS_04_P01
- P1 pad 12: /Level Shifters/PAN5V.CS_05 -> /Panel Headers/CS_05_P01
- P1 pad 13: /Level Shifters/PAN5V.CS_06 -> /Panel Headers/CS_06_P01
- P1 pad 14: /Level Shifters/PAN5V.CS_07 -> /Panel Headers/CS_07_P01
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
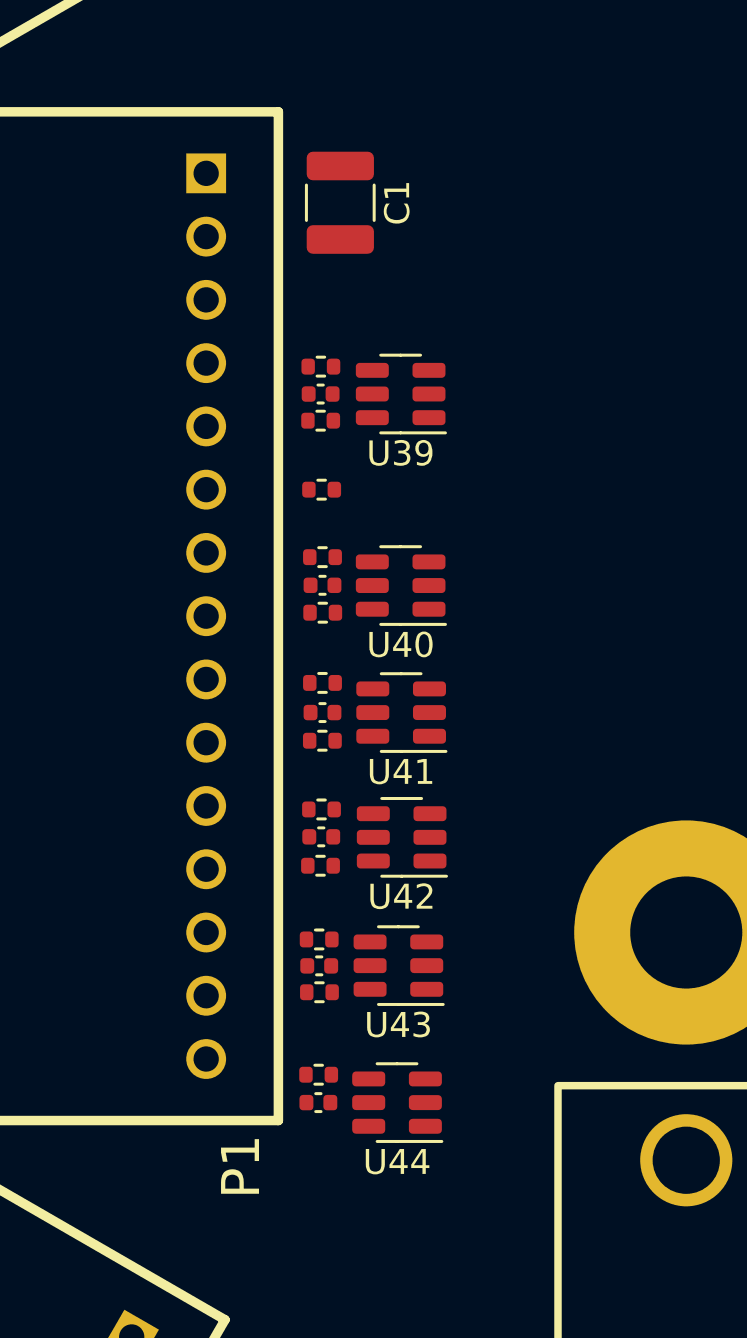
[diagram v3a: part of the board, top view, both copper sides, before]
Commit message: Worked on 12-12 NI arena with schmitt buffers.
Finalized layout of components at base of panel columns.
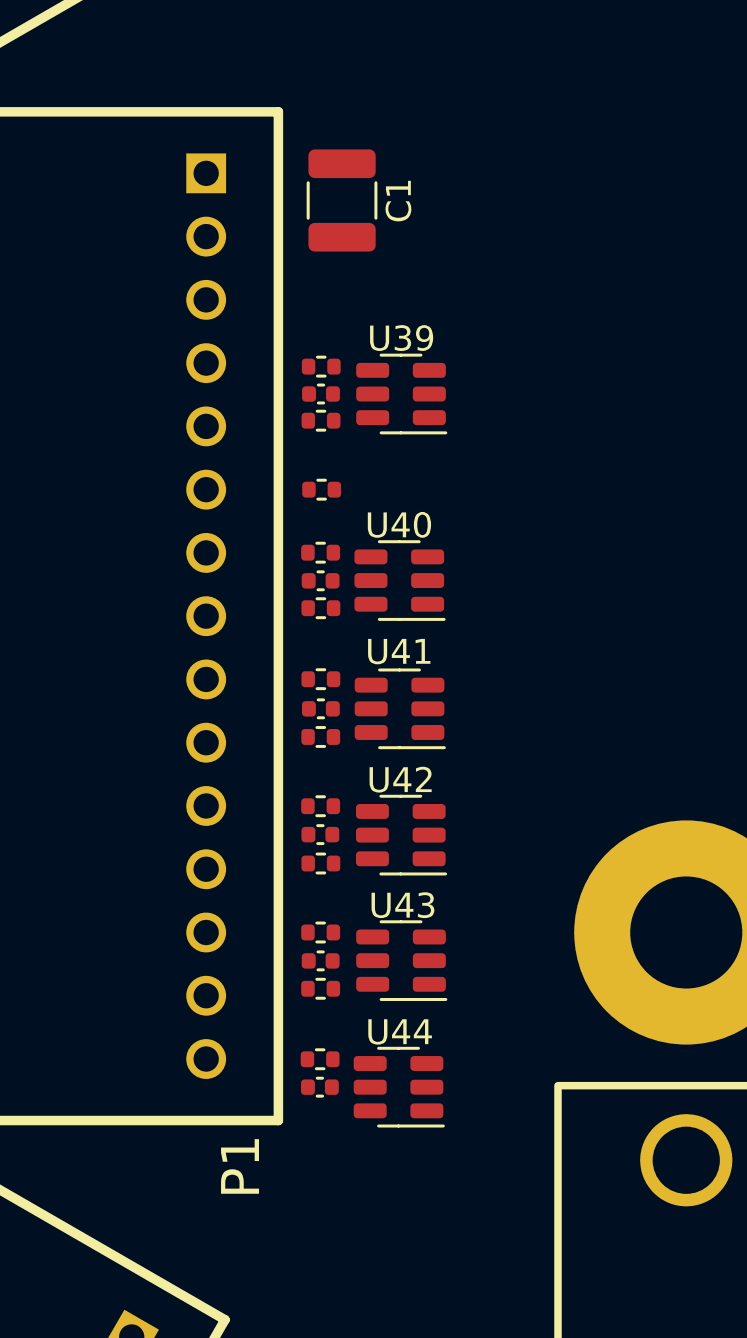
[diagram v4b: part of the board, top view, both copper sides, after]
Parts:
- moved C40 0.62 mm to (271.0, 196.7)
- moved R40 0.62 mm to (271.1, 195.6)
- moved U44 0.62 mm to (274.2, 196.7)
- moved R38 0.29 mm to (271.1, 190.5)
- moved U43 0.23 mm to (274.3, 191.6)
- moved C39 0.21 mm to (271.1, 191.6)
- moved U40 0.21 mm to (274.2, 176.4)
- moved C36 0.20 mm to (271.1, 176.4)
- moved R32 0.20 mm to (271.1, 175.2)
- moved R33 0.20 mm to (271.1, 177.5)
- moved R35 0.16 mm to (271.1, 182.7)
- moved C37 0.16 mm to (271.1, 181.5)
- moved R34 0.16 mm to (271.1, 180.3)
- moved U41 0.16 mm to (274.2, 181.5)
- moved R39 0.15 mm to (271.1, 192.8)
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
